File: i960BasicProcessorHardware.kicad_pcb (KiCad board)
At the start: 4 copper layers, 169.9 x 169.8 mm, 88 parts, among them J1 Conn_01x08, J10 Conn_02x39_Odd_Even, J11 Conn_02x09_Odd_Even, J12 Conn_01x03, J13 AVR-ISP-6, J14 Conn_01x06 (Serial Connector), J15 Conn_02x08_Odd_Even, J16 Conn_02x08_Odd_Even, J17 Conn_02x08_Odd_Even, J18 Conn_02x09_Odd_Even, J19 Conn_02x16_Odd_Even, J2 Conn_02x05_Odd_Even, J20 Conn_02x08_Odd_Even, J22 Conn_01x03, J23 AVR-ISP-6, J24 Conn_01x06 (Serial Connector), J3 Conn_02x05_Odd_Even, J4 Conn_02x05_Odd_Even, J5 Conn_02x16_Odd_Even, J6 Conn_01x03, J7 Conn_01x03, J8 Conn_01x03, J9 Conn_01x11, U1 74HC245, U10 Adafruit_FeatherWing (PSRAM F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, U11 Adafruit_FeatherWing (PSRAM F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, U12 74LS125, U13 74LS04, U14 74LS08, U15 74LS174, U16 SN74LVC245AN, U17 74LS174, U18 ATmega1284P-PU, U19 ATmega1284P-PU, U2 80960Sx, U3 MCP23S17_SP, U4 MCP23S17_SP, U5 74HC245, U6 74HC573, U7 74HC573, U8 MCP23S17_SP, U9 MCP23S17_SP, X1 CXO_DIP14

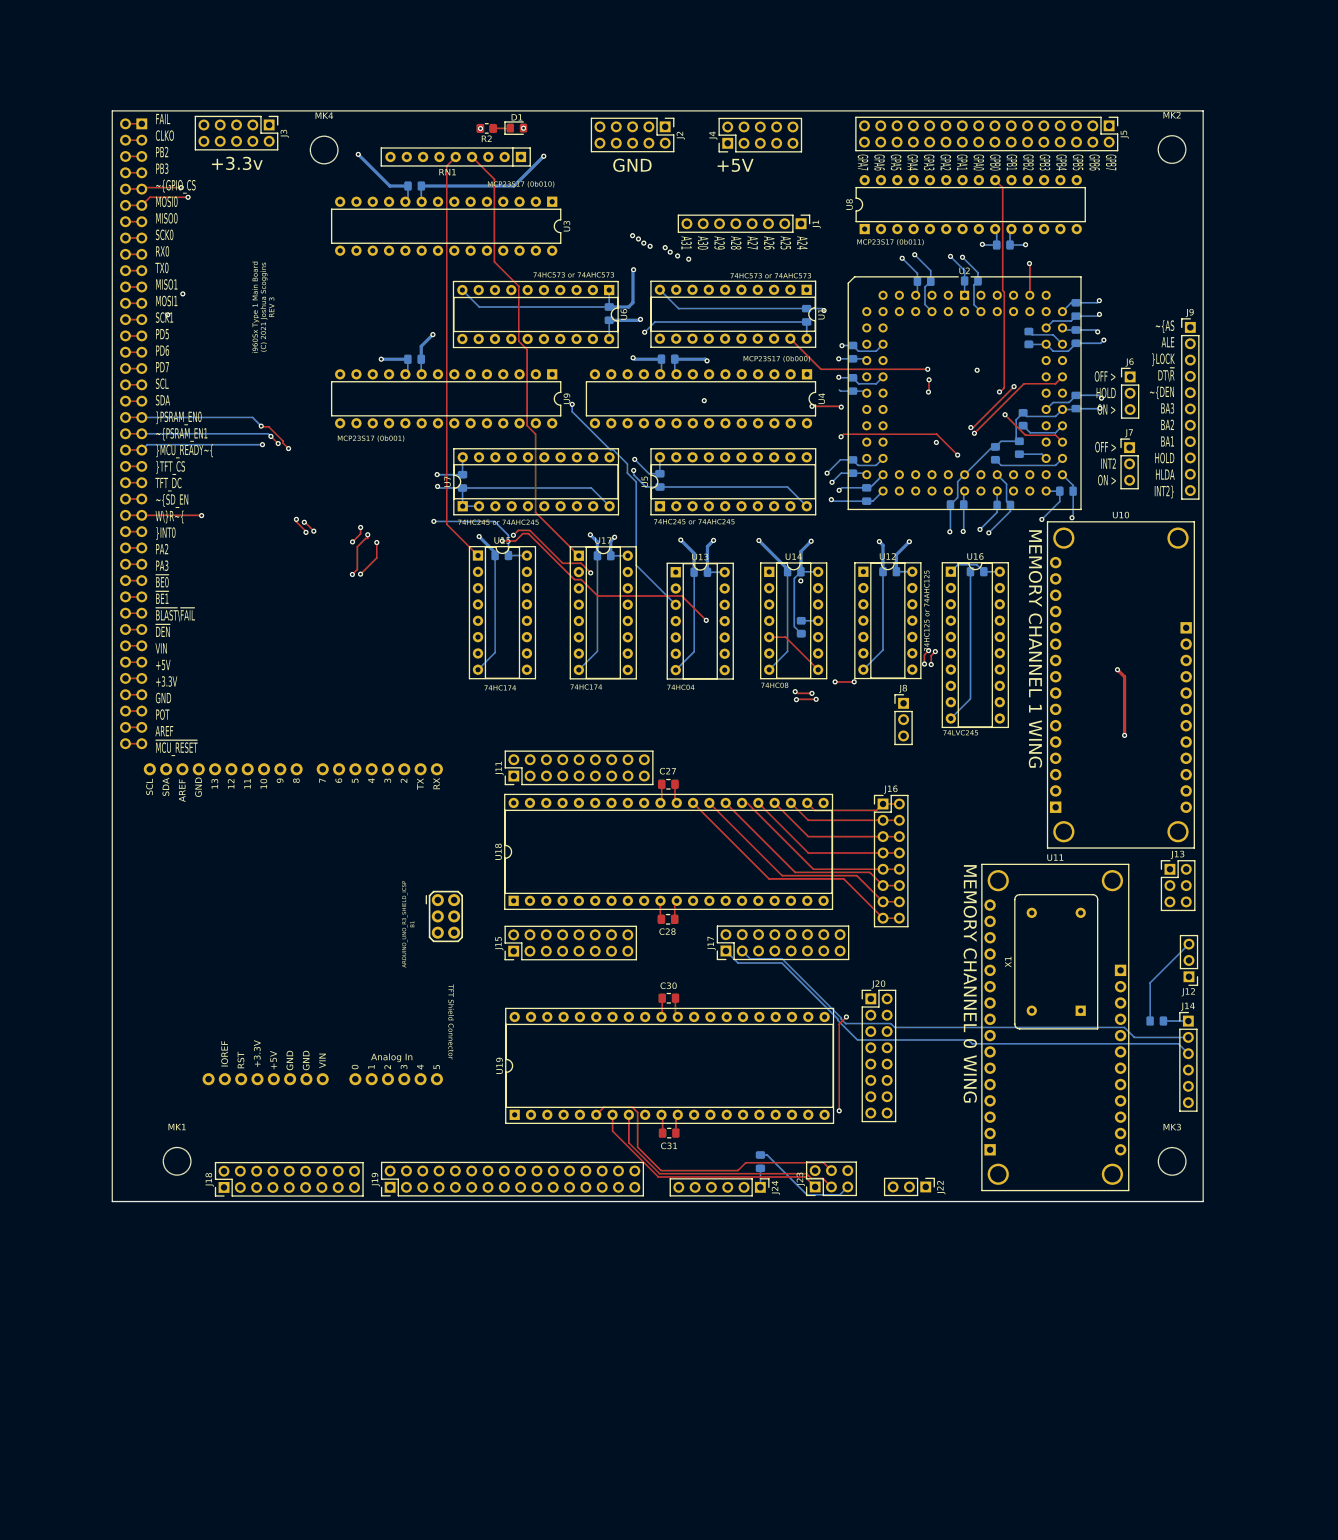
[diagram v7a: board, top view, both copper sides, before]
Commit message: Finish cleaning up rev3 for now the layout is complete
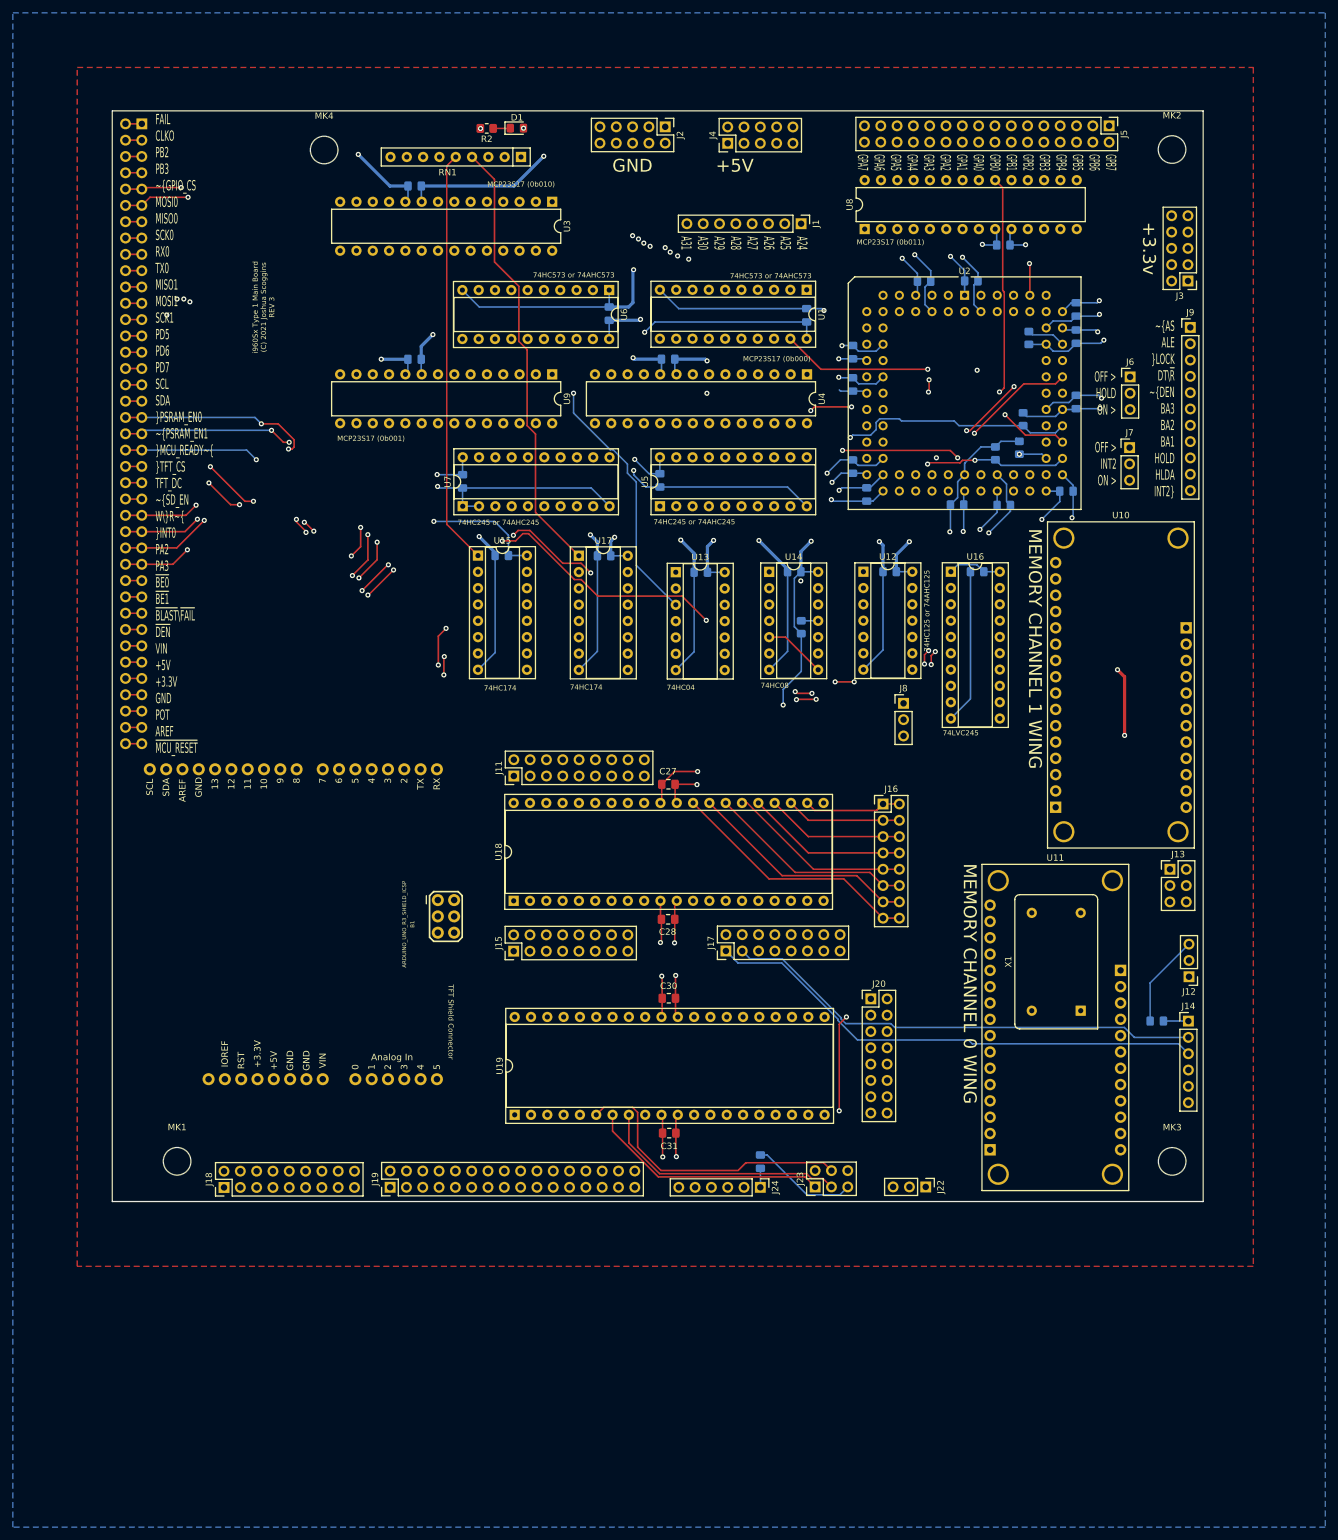
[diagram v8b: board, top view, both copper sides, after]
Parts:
- moved J3 145.1 mm to (184.5, 56.5), turned to 180 degrees
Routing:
- net /~RESET960: track 13.8 -> 169.6 mm, vias 0 -> 3
- net /~INT0: track 6.99 -> 162.3 mm, vias 0 -> 2
- net /~INT3: track 9.58 -> 163.1 mm, vias 0 -> 2
- net /RX0: track 2.54 -> 107.6 mm, vias 0 -> 3
- net /TX0: track 2.54 -> 104.5 mm, vias 0 -> 3
- net /~MCU_RESET: track 206.7 -> 306.1 mm
- net /VIN: track 2.54 -> 96.4 mm
- net /~SD_CS: track 2.54 -> 71.5 mm
- net /TFT_DC: track 2.54 -> 67.6 mm, vias 0 -> 2
- net /SCL: track 2.54 -> 66.5 mm
- net /~TFT_CS: track 2.54 -> 65.1 mm, vias 0 -> 2
- net /SDA: track 2.54 -> 63.1 mm
- net /SCK0: track 355.1 -> 401.4 mm, vias 4 -> 6
- net /MISO0: track 352.9 -> 398.6 mm, vias 4 -> 6
- net /MOSI0: track 358.4 -> 394.2 mm
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- added copper zone on In2.Cu, net +3V3
- added copper zone on F.Cu, net +5V
- added copper zone on B.Cu, net GND
